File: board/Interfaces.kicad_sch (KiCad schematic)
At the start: 21 parts, among them U2 SN65HVD232

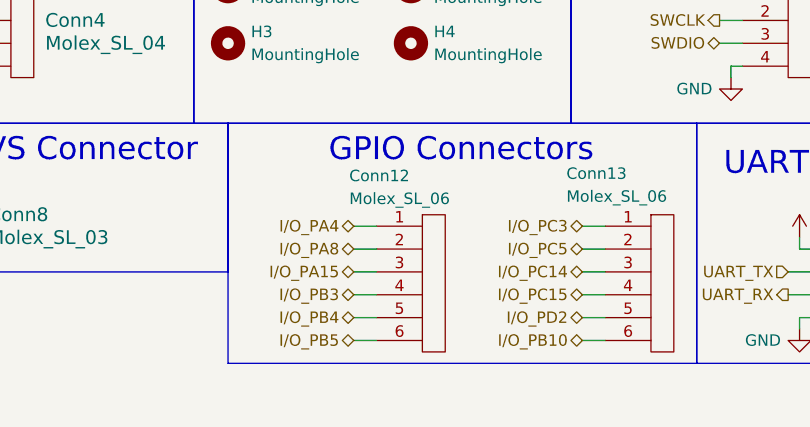
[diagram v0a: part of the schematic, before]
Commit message: First draft of wiring for the layout finished.
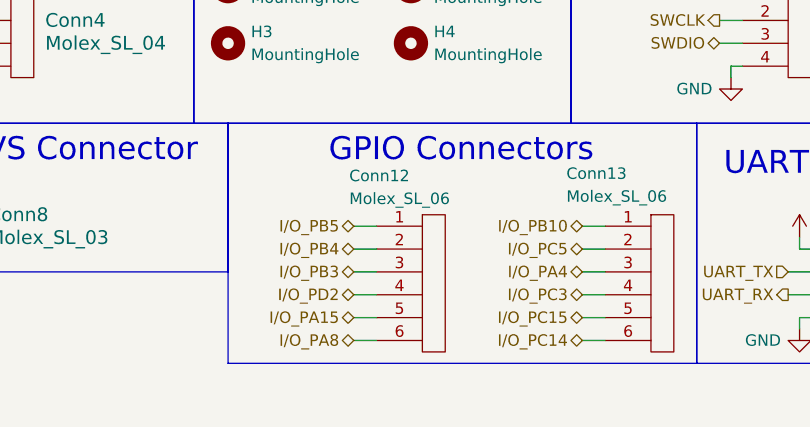
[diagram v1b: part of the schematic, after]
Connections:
- net I/O_PA15: now also Conn12.5; no longer Conn12.3
- net I/O_PA4: now also Conn13.3; no longer Conn12.1
- net I/O_PA8: now also Conn12.6; no longer Conn12.2
- net I/O_PB10: now also Conn13.1; no longer Conn13.6
- net I/O_PB3: now also Conn12.3; no longer Conn12.4
- net I/O_PB4: now also Conn12.2; no longer Conn12.5
- net I/O_PB5: now also Conn12.1; no longer Conn12.6
- net I/O_PC14: now also Conn13.6; no longer Conn13.3
- net I/O_PC15: now also Conn13.5; no longer Conn13.4
- net I/O_PC3: now also Conn13.4; no longer Conn13.1
- net I/O_PD2: now also Conn12.4; no longer Conn13.5

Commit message: Tentatively finished rev1.
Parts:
- removed Conn14, Conn15, Conn16: Molex_SL_03, MRDT_Connectors:MOLEX_SL_03_Vertical, symbol MRDT_Connectors:Molex_SL_03
- added J1, J2, J3: Conn_01x03, Connector_PinSocket_1.00mm:PinSocket_1x03_P1.00mm_Vertical, symbol Connector_Generic:Conn_01x03
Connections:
- net TEST_OPN_U: now also J1.3 (Pin_3)
- net TEST_OPN_V: now also J2.3 (Pin_3)
- net TEST_OPN_W: now also J3.3 (Pin_3)
- net TEST_OPO_U: now also J1.2 (Pin_2)
- net TEST_OPO_V: now also J2.2 (Pin_2)
- net TEST_OPO_W: now also J3.2 (Pin_2)
- net TEST_OPP_U: now also J1.1 (Pin_1)
- net TEST_OPP_V: now also J2.1 (Pin_1)
- net TEST_OPP_W: now also J3.1 (Pin_1)
- net CANH renamed CAN+
- net CANL renamed CAN-
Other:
- moved on the sheet: R6, U2

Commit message: Fixed many issues found in Rev1 review prior to order
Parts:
- J1, J2, J3: footprint Connector_PinSocket_1.00mm:PinSocket_1x03_P1.00mm_Vertical -> Connector_PinSocket_2.54mm:PinSocket_1x03_P2.54mm_Vertical
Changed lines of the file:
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@@
 			)
 		)
-		(property "Footprint" "Connector_PinSocket_1.00mm:PinSocket_1x03_P1.00mm_Vertical"
+		(property "Footprint" "Connector_PinSocket_2.54mm:PinSocket_1x03_P2.54mm_Vertical"
 			(at 34.29 66.04 0)
 			(effects
@@
 			)
 		)
-		(property "Footprint" "Connector_PinSocket_1.00mm:PinSocket_1x03_P1.00mm_Vertical"
+		(property "Footprint" "Connector_PinSocket_2.54mm:PinSocket_1x03_P2.54mm_Vertical"
 			(at 116.84 66.04 0)
 			(effects
@@
 			)
 		)
-		(property "Footprint" "Connector_PinSocket_1.00mm:PinSocket_1x03_P1.00mm_Vertical"
+		(property "Footprint" "Connector_PinSocket_2.54mm:PinSocket_1x03_P2.54mm_Vertical"
 			(at 76.2 66.04 0)
 			(effects
